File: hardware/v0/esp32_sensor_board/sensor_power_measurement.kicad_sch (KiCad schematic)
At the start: 0 parts

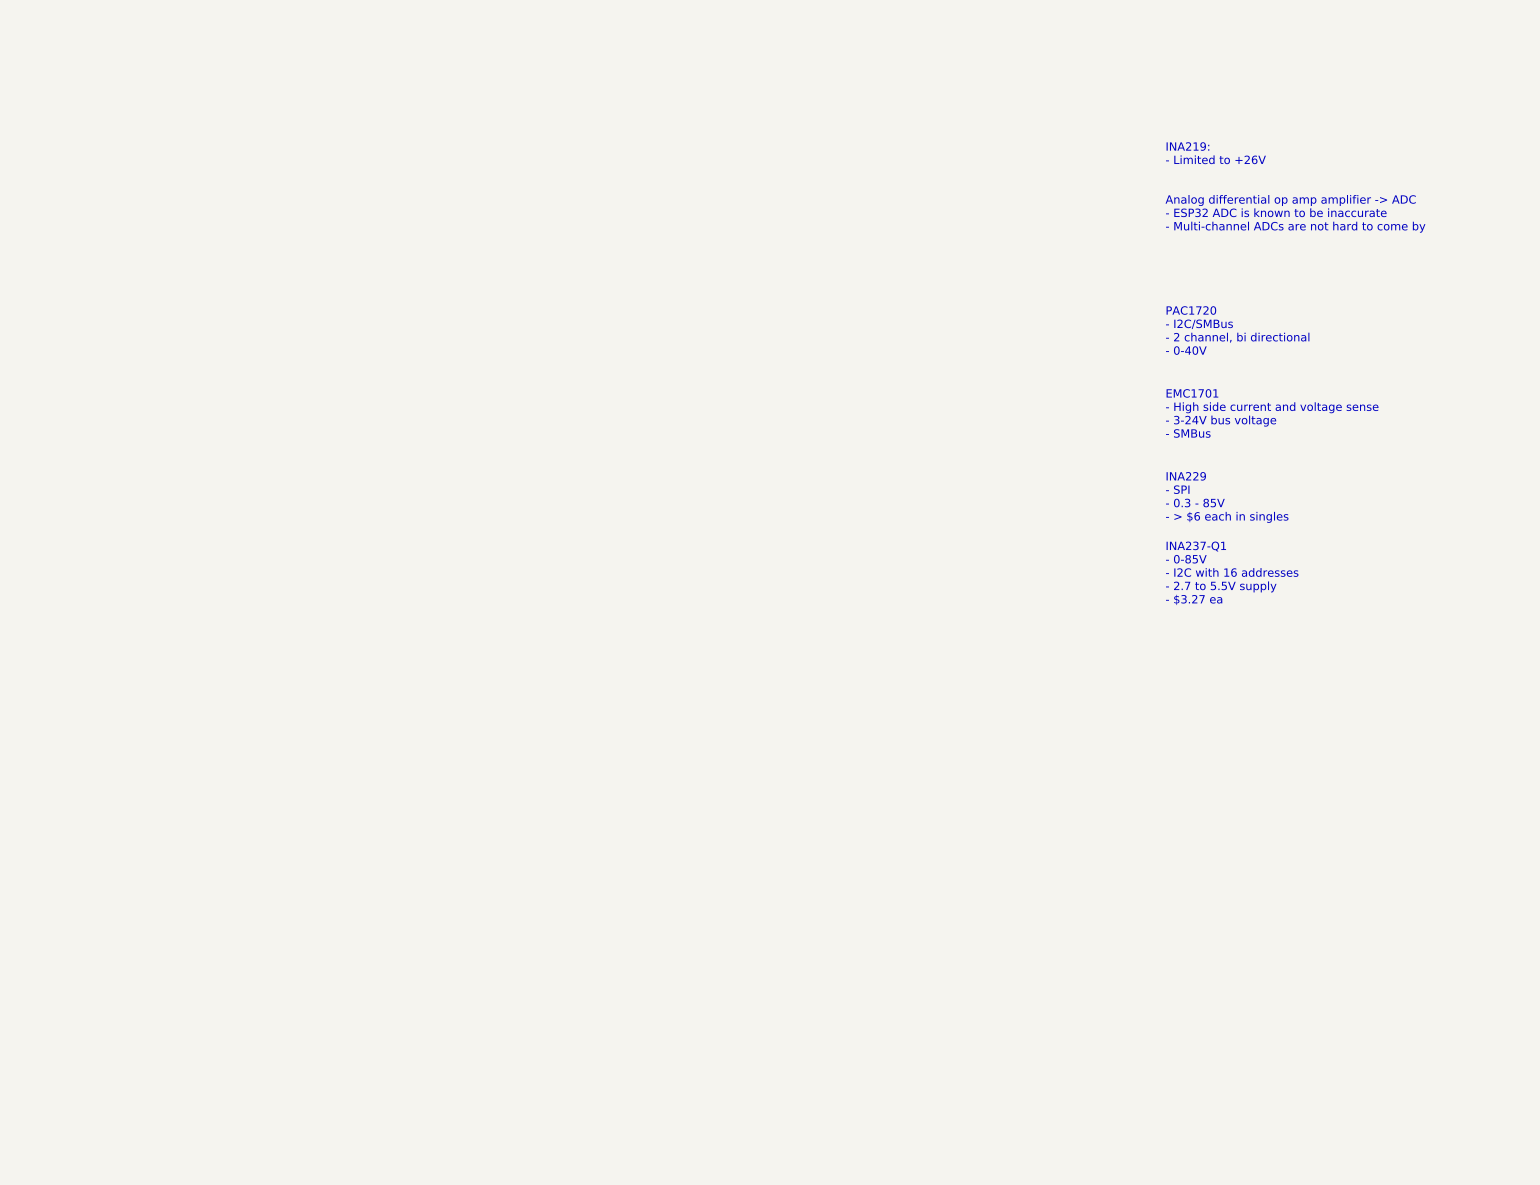
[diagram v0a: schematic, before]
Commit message: PCB ordered, a few initial mistakes fixed
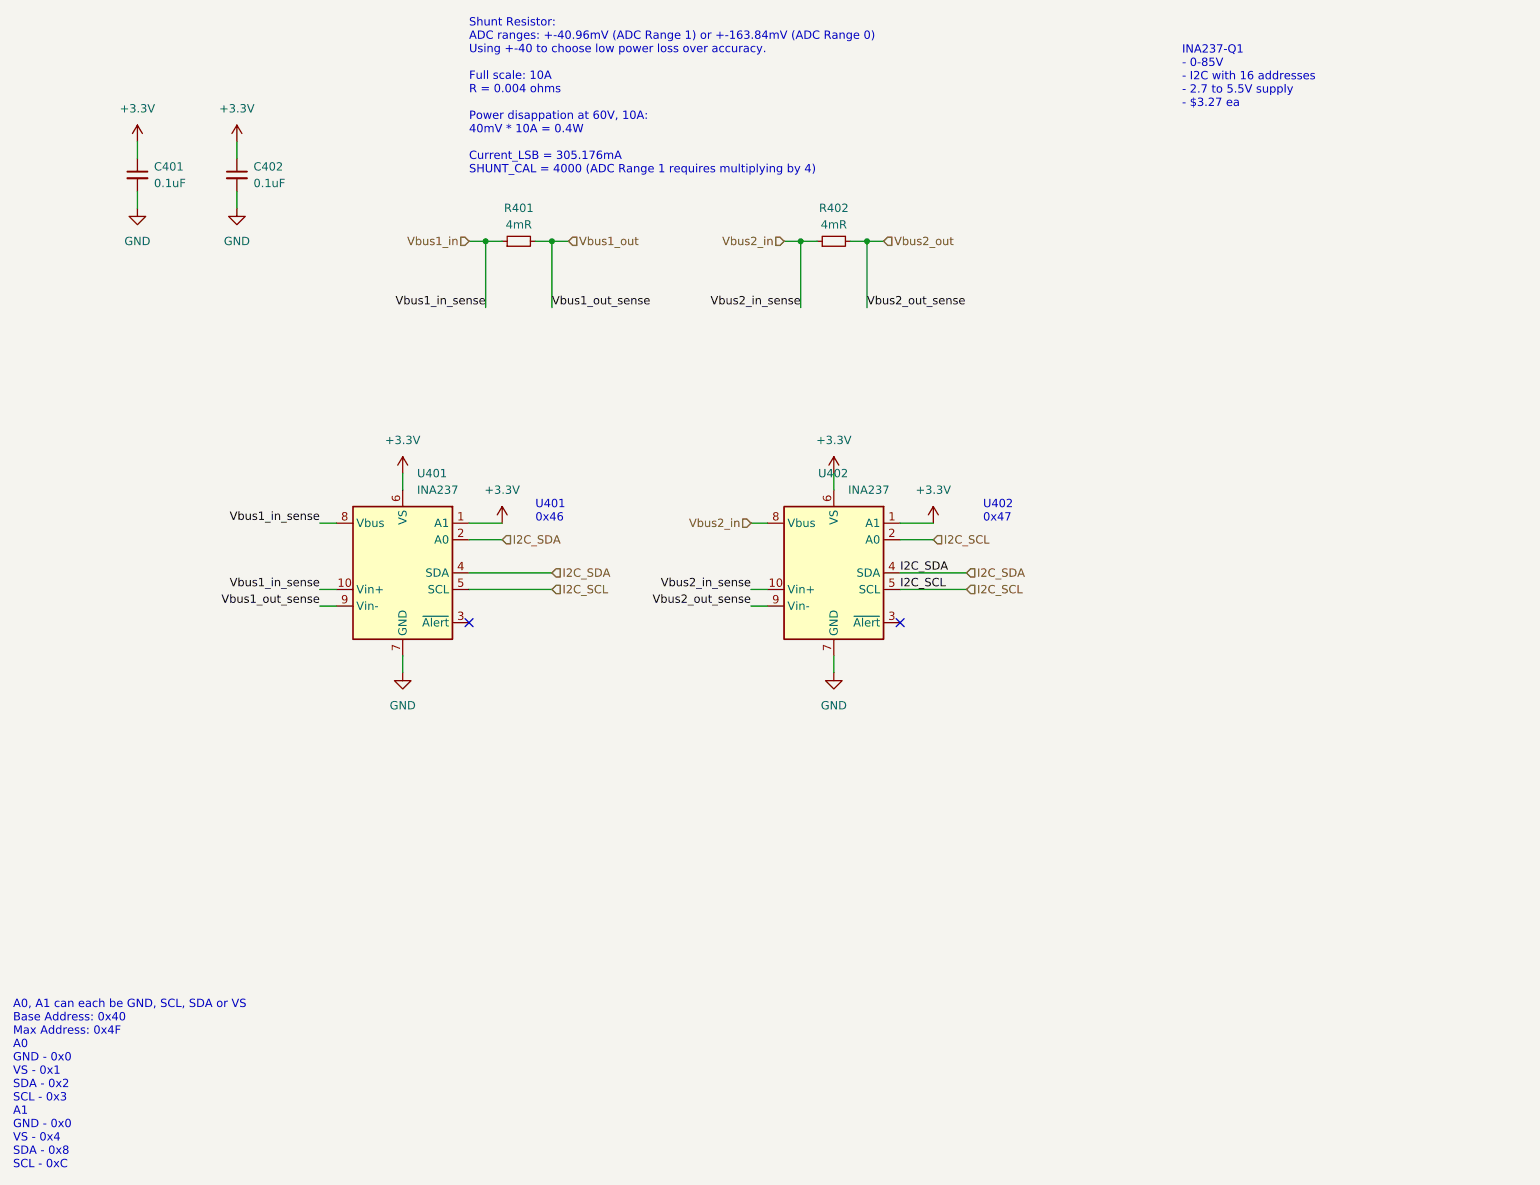
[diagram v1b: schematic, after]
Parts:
- added C401, C402: 0.1uF, Capacitor_SMD:C_0603_1608Metric, symbol Device:C_Small
- added R401, R402: 4mR, Resistor_SMD:R_2512_6332Metric, symbol Device:R_Small
- added U401, U402: INA237, Package_SO:VSSOP-10_3x3mm_P0.5mm, symbol BVH_Power:INA237
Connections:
- new net +3.3V: C401.1, C402.1, U401.1 (A1), U401.6 (VS), U402.1 (A1), U402.6 (VS)
- new net GND: C401.2, C402.2, U401.7 (GND), U402.7 (GND)
- new net I2C_SCL: U401.5 (SCL), U402.2 (A0), U402.5 (SCL)
- new net I2C_SDA: U401.2 (A0), U401.4 (SDA), U402.4 (SDA)
- new net Vbus1_in: R401.1, U401.10 (Vin+), U401.8 (Vbus)
- new net Vbus1_out: R401.2, U401.9 (Vin-)
- new net Vbus2_in: R402.1, U402.10 (Vin+), U402.8 (Vbus)
- new net Vbus2_out: R402.2, U402.9 (Vin-)
- no-connect marks 0 -> 2
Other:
- note added: "A0, A1 can each be GND, SCL, SDA or VS Base Address: 0x40 Max Address: 0x4F A0 GND - 0x0 VS - 0x1 SDA - 0x2 SCL - 0x3 A1 GND - 0x0 VS - 0x4 SDA - 0x8 SCL - 0xC"
- note added: "Shunt Resistor: ADC ranges: +-40.96mV (ADC Range 1) or +-163.84mV (ADC Range 0) Using +-40 to choose low power loss over accuracy. Full scale: 10A R = 0.004 ohms Power disappation at 60V, 10A: 40mV * 10A = 0.4W Current_LSB = 305.176mA SHUNT_CAL = 4000 (ADC Range 1 requires multiplying by 4)"
- note added: "U401 0x46"
- note added: "U402 0x47"
- note removed: "Analog differential op amp amplifier -> ADC - ESP32 ADC is known to be inaccurate - Multi-channel ADCs are not hard to come by"
- note removed: "EMC1701 - High side current and voltage sense - 3-24V bus voltage - SMBus"
- note removed: "INA219: - Limited to +26V"
- note removed: "INA229 - SPI - 0.3 - 85V - > $6 each in singles"
- note removed: "PAC1720 - I2C/SMBus - 2 channel, bi directional - 0-40V"
